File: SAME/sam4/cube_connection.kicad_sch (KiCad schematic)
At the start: 1 part

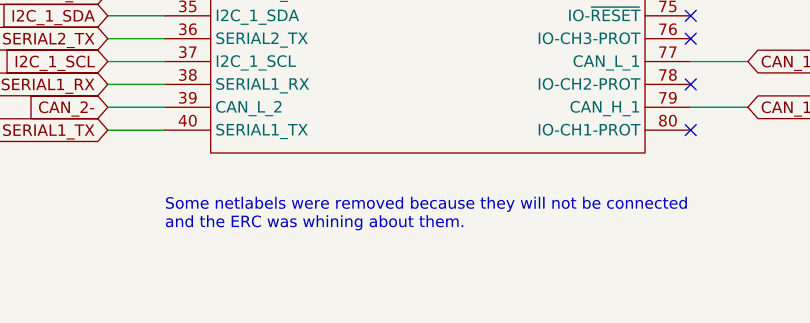
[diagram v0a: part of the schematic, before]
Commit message: add JLC ordering files. small tweaks
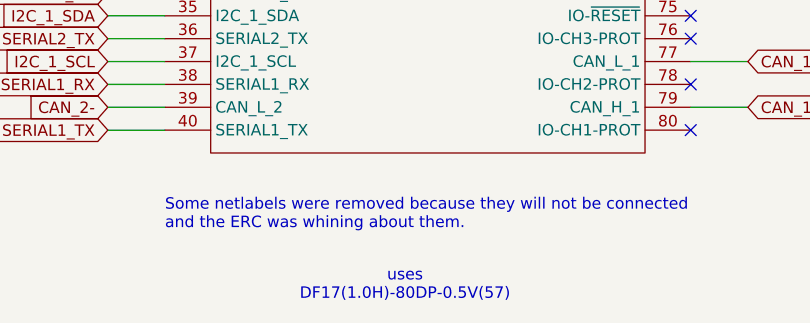
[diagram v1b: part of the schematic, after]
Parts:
- Pix1: LCSC (none) -> C354837
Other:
- note added: "uses DF17(1.0H)-80DP-0.5V(57)"
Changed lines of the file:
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@@
+		)
+	)
+	(text "uses\nDF17(1.0H)-80DP-0.5V(57)"
+		(exclude_from_sim no)
+		(at 142.24 160.782 0)
+		(effects
+			(font
+				(size 1.27 1.27)
+			)
 		)
 	)
@@
 			)
 		)
-		(property "LCSC" ""
+		(property "LCSC" "C354837"
 			(at 144.78 39.37 0)
 			(effects
